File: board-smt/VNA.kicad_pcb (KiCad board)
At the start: 2 copper layers, 100 x 85 mm, 185 parts, among them J1 Conn_02x07_Odd_Even, J10 Conn_01x04, J11 Conn_01x01, J13 Barrel_Jack, J14 Conn_01x01, J15 Conn_01x02, J16 Conn_01x01, J18 Conn_01x01, J19 Conn_01x01, J2 Conn_Coaxial, J20 Conn_01x01, J21 Conn_01x01, J24 USB_B, J3 Conn_01x04, J8 Conn_01x01, J9 Conn_Coaxial, Q3 2SC3356, SW1 SW_DPDT_x2, SW2 SW_DIP_x01, U1 SI5351A, U10 MT3608, U11 CN3052, U12 SI5351A, U13 MicroSD_SPI_CD, U14 STM32F103C8T6, U2 LM393, U3 SA612, U4 SA612, U5 SA612, U6 LM358, U7 LM358, U8 AMS1117-3V3, U9 78M05_TO252, Y1 25 MHz, Y2 8 MHz

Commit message: Submitted to JLCPCB 2020-07-12
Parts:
- removed G***: LOGO, VNA:VNAOMizer
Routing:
- net GND: track 1891.0 -> 1892.7 mm
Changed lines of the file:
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@@
     (links 377)
     (no_connects 0)
-    (area 49.924999 49.924999 150.075001 135.075001)
+    (area 48.252381 38.824999 153.542859 144.065001)
     (thickness 1.6)
     (drawings 46)
     (tracks 3988)
     (zones 0)
-    (modules 185)
+    (modules 184)
     (nets 117)
   )
@@
   )
   (setup
-    (last_trace_width 0.35)
+    (last_trace_width 0.25)
     (user_trace_width 0.35)
     (user_trace_width 0.5)
@@
     (tags "capacitor 0805")
     (attr smd)
-    (fp_text reference C9 (at 1.7 1.7 360) (layer F.SilkS)
+    (fp_text reference C9 (at 2.89 0.13 360) (layer F.SilkS)
       (effects (font (size 1 1) (thickness 0.15)))
     )
@@
     (tags "capacitor 0805")
     (attr smd)
-    (fp_text reference C43 (at 3.048 -0.254 180) (layer F.SilkS)
+    (fp_text reference C43 (at 0.04 1.744 270) (layer F.SilkS)
       (effects (font (size 1 1) (thickness 0.15)))
     )
@@
     )
   )
-  (module VNA:VNAOMizer (layer F.Cu)
-    (at 113 96.3)
-    (fp_text reference G*** (at 0 0) (layer F.SilkS) hide
-      (effects (font (thickness 0.3)))
-    )
-    (fp_text value LOGO (at 0.75 0) (layer F.SilkS) hide
-      (effects (font (thickness 0.3)))
-    )
-    (fp_poly (pts (xy 0.293123 -4.621389) (xy 0.317894 -4.398101) (xy 0.334924 -4.059111) (xy 0.344295 -3.629613)
-      (xy 0.34609 -3.134799) (xy 0.340391 -2.599861) (xy 0.327282 -2.049993) (xy 0.306845 -1.510387)
-      (xy 0.281376 -1.040503) (xy 0.132851 0.549482) (xy -0.105598 2.051599) (xy -0.329137 3.068511)
-      (xy -0.44618 3.524507) (xy -0.548457 3.872163) (xy -0.646898 4.141893) (xy -0.752432 4.364109)
-      (xy -0.859182 4.543478) (xy -0.990915 4.742234) (xy -1.086976 4.877522) (xy -1.128467 4.922866)
-      (xy -1.128889 4.921308) (xy -1.107542 4.840305) (xy -1.050995 4.66136) (xy -0.970491 4.419781)
-      (xy -0.951308 4.363564) (xy -0.898844 4.199208) (xy -0.851171 4.020657) (xy -0.806283 3.813472)
-      (xy -0.76217 3.563215) (xy -0.716825 3.255448) (xy -0.668239 2.875732) (xy -0.614404 2.40963)
-      (xy -0.553313 1.842704) (xy -0.482956 1.160514) (xy -0.422889 0.564444) (xy -0.332038 -0.538475)
-      (xy -0.293424 -1.515472) (xy -0.307325 -2.371822) (xy -0.374021 -3.1128) (xy -0.49379 -3.743681)
-      (xy -0.666911 -4.269739) (xy -0.680017 -4.300431) (xy -0.776027 -4.552624) (xy -0.816049 -4.729629)
-      (xy -0.80382 -4.798291) (xy -0.705213 -4.833254) (xy -0.507852 -4.863601) (xy -0.254079 -4.882859)
-      (xy -0.248985 -4.883076) (xy 0.2416 -4.903612) (xy 0.293123 -4.621389)) (layer F.SilkS) (width 0.01))
-    (fp_poly (pts (xy 0.668263 1.317823) (xy 0.82314 1.450533) (xy 1.041855 1.651986) (xy 1.308286 1.906042)
-      (xy 1.606316 2.196557) (xy 1.919825 2.507389) (xy 2.232692 2.822398) (xy 2.5288 3.12544)
-      (xy 2.792028 3.400373) (xy 3.006256 3.631056) (xy 3.155366 3.801346) (xy 3.223238 3.895102)
-      (xy 3.225398 3.905751) (xy 3.182105 3.970047) (xy 3.099226 3.976528) (xy 2.956451 3.918004)
-      (xy 2.733471 3.787287) (xy 2.540815 3.663418) (xy 2.271595 3.49674) (xy 1.919779 3.292474)
-      (xy 1.529298 3.075503) (xy 1.144085 2.87071) (xy 1.112065 2.854184) (xy 0.211667 2.390755)
-      (xy 0.211667 2.035297) (xy 0.243772 1.767589) (xy 0.32785 1.526408) (xy 0.445544 1.34856)
-      (xy 0.578497 1.270853) (xy 0.593341 1.27) (xy 0.668263 1.317823)) (layer F.SilkS) (width 0.01))
-    (fp_poly (pts (xy -0.946216 1.065488) (xy -0.900925 1.10942) (xy -0.896299 1.223823) (xy -0.922406 1.442396)
-      (xy -0.924452 1.457488) (xy -0.981931 1.726207) (xy -1.064968 1.924752) (xy -1.10667 1.978735)
-      (xy -1.230238 2.049751) (xy -1.462247 2.143052) (xy -1.773553 2.249581) (xy -2.135011 2.360284)
-      (xy -2.517475 2.466105) (xy -2.891801 2.557989) (xy -3.139722 2.610395) (xy -3.407776 2.668996)
-      (xy -3.736706 2.750557) (xy -4.078508 2.84215) (xy -4.385181 2.930848) (xy -4.608723 3.003724)
-      (xy -4.630389 3.011827) (xy -4.715506 3.006539) (xy -4.727222 2.976652) (xy -4.750819 2.849293)
-      (xy -4.767361 2.799718) (xy -4.751137 2.730729) (xy -4.640454 2.649848) (xy -4.418805 2.54681)
-      (xy -4.255833 2.481694) (xy -3.959586 2.360263) (xy -3.572416 2.19175) (xy -3.129516 1.99238)
-      (xy -2.666076 1.778374) (xy -2.217289 1.565958) (xy -1.818347 1.371353) (xy -1.541823 1.23054)
-      (xy -1.318736 1.13034) (xy -1.1183 1.068245) (xy -1.042105 1.058333) (xy -0.946216 1.065488)) (layer F.SilkS) (width 0.01))
-    (fp_poly (pts (xy -0.542509 -1.64788) (xy -0.521421 -1.549341) (xy -0.530529 -1.363452) (xy -0.56247 -1.138882)
-      (xy -0.609884 -0.924303) (xy -0.665407 -0.768384) (xy -0.679048 -0.745207) (xy -0.798112 -0.65308)
-      (xy -1.042072 -0.532947) (xy -1.398515 -0.389323) (xy -1.855024 -0.226725) (xy -2.399185 -0.04967)
-      (xy -3.018582 0.137325) (xy -3.421944 0.252633) (xy -3.804445 0.360157) (xy -4.142102 0.455712)
-      (xy -4.410267 0.532274) (xy -4.584297 0.582817) (xy -4.636768 0.598905) (xy -4.747126 0.577683)
-      (xy -4.770388 0.551681) (xy -4.777941 0.491533) (xy -4.724056 0.417029) (xy -4.596658 0.320843)
-      (xy -4.38367 0.195646) (xy -4.073018 0.034112) (xy -3.652626 -0.171087) (xy -3.316111 -0.330735)
-      (xy -2.868776 -0.543522) (xy -2.396326 -0.771903) (xy -1.941683 -0.994892) (xy -1.54777 -1.191506)
-      (xy -1.367319 -1.283497) (xy -1.066596 -1.433976) (xy -0.812523 -1.552478) (xy -0.630213 -1.62791)
-      (xy -0.544776 -1.649177) (xy -0.542509 -1.64788)) (layer F.SilkS) (width 0.01))
-    (fp_poly (pts (xy 0.731539 -1.46223) (xy 0.818222 -1.415777) (xy 1.020676 -1.333993) (xy 1.319994 -1.223676)
-      (xy 1.69727 -1.091624) (xy 2.1336 -0.944634) (xy 2.54 -0.811992) (xy 3.1671 -0.606363)
-      (xy 3.667291 -0.433407) (xy 4.050033 -0.289514) (xy 4.324785 -0.171074) (xy 4.501006 -0.074478)
-      (xy 4.533195 -0.051462) (xy 4.689368 0.081748) (xy 4.784372 0.186969) (xy 4.797778 0.217595)
-      (xy 4.741426 0.270517) (xy 4.610175 0.272792) (xy 4.460733 0.22468) (xy 4.445 0.215962)
-      (xy 4.245346 0.135201) (xy 3.909109 0.045705) (xy 3.440487 -0.051644) (xy 2.843679 -0.155962)
-      (xy 2.222161 -0.251889) (xy 1.762746 -0.320933) (xy 1.421289 -0.377361) (xy 1.175812 -0.426708)
-      (xy 1.004335 -0.474508) (xy 0.884877 -0.526294) (xy 0.795458 -0.587601) (xy 0.758473 -0.620418)
-      (xy 0.608861 -0.816858) (xy 0.564488 -1.055794) (xy 0.564445 -1.065764) (xy 0.58005 -1.332126)
-      (xy 0.624665 -1.477904) (xy 0.694992 -1.495271) (xy 0.731539 -1.46223)) (layer F.SilkS) (width 0.01))
-  )
   (gr_text "AMS1117-\n3V3" (at 144.8 97.2 90) (layer F.SilkS)
     (effects (font (size 1 1) (thickness 0.15)))
@@
     (effects (font (size 1 1) (thickness 0.15)))
   )
-  (gr_text "VNA-O-MIZER BY D MARKS KW4TI,\nLICENSED UNDER CC-BY-SA 4.0" (at 83.9 103.3) (layer F.SilkS)
+  (gr_text "VNA-O-MIZER\nBY D MARKS KW4TI,\nLICENSED UNDER\nCC-BY-SA 4.0" (at 108.1 62.9) (layer F.SilkS)
     (effects (font (size 1 1) (thickness 0.15)))
   )
@@
   (via (at 60.4 70.8) (size 0.6) (drill 0.4) (layers F.Cu B.Cu) (net 2))
   (segment (start 60.45 70.95) (end 60.4 70.8) (width 0.35) (layer F.Cu) (net 2))
-  (segment (start 74.7 76.35) (end 74.65 77.55) (width 0.35) (layer F.Cu) (net 2))
-  (via (at 74.6 77.6) (size 0.6) (drill 0.4) (layers F.Cu B.Cu) (net 2))
-  (segment (start 74.65 77.55) (end 74.6 77.6) (width 0.35) (layer F.Cu) (net 2))
+  (segment (start 74.7 76.35) (end 73.57 76.45) (width 0.35) (layer F.Cu) (net 2))
+  (via (at 73.52 76.5) (size 0.6) (drill 0.4) (layers F.Cu B.Cu) (net 2))
+  (segment (start 73.57 76.45) (end 73.52 76.5) (width 0.35) (layer F.Cu) (net 2))
   (segment (start 74.7 76.35) (end 75.35 76.35) (width 0.35) (layer F.Cu) (net 2))
   (via (at 75.8 76.8) (size 0.6) (drill 0.4) (layers F.Cu B.Cu) (net 2))
@@
   (via (at 96.6 119.5) (size 0.6) (drill 0.4) (layers F.Cu B.Cu) (net 2))
   (segment (start 85.45 121.45) (end 84.62 121.45) (width 0.35) (layer F.Cu) (net 2))
-  (segment (start 84.348 107.97) (end 84.836 108.458) (width 0.5) (layer F.Cu) (net 2))
-  (via (at 84.836 108.458) (size 0.6) (drill 0.4) (layers F.Cu B.Cu) (net 2))
+  (segment (start 84.348 107.97) (end 84.84 107.38) (width 0.5) (layer F.Cu) (net 2))
+  (via (at 84.84 107.38) (size 0.6) (drill 0.4) (layers F.Cu B.Cu) (net 2))
   (segment (start 83.566 107.97) (end 84.348 107.97) (width 0.5) (layer F.Cu) (net 2))
   (via (at 85.45 121.45) (size 0.6) (drill 0.4) (layers F.Cu B.Cu) (net 2))
@@
   (segment (start 85.3 111.15) (end 85.2 111.25) (width 0.35) (layer B.Cu) (net 2))
   (via (at 85.3 111.15) (size 0.6) (drill 0.4) (layers F.Cu B.Cu) (net 2))
-  (segment (start 85.2 109.4) (end 85.3 111.15) (width 0.35) (layer F.Cu) (net 2))
-  (segment (start 85.3 109.3) (end 85.2 109.4) (width 0.35) (layer F.Cu) (net 2))
-  (via (at 85.3 109.3) (size 0.6) (drill 0.4) (layers F.Cu B.Cu) (net 2))
-  (segment (start 84.958 108.458) (end 85.3 109.3) (width 0.35) (layer B.Cu) (net 2))
-  (segment (start 84.836 108.458) (end 84.958 108.458) (width 0.35) (layer B.Cu) (net 2))
+  (segment (start 86.23 109.31) (end 85.3 111.15) (width 0.35) (layer F.Cu) (net 2))
+  (segment (start 86.33 109.21) (end 86.23 109.31) (width 0.35) (layer F.Cu) (net 2))
+  (via (at 86.33 109.21) (size 0.6) (drill 0.4) (layers F.Cu B.Cu) (net 2))
+  (segment (start 84.962 107.38) (end 86.33 109.21) (width 0.35) (layer B.Cu) (net 2))
+  (segment (start 84.84 107.38) (end 84.962 107.38) (width 0.35) (layer B.Cu) (net 2))
   (segment (start 84.62 121.45) (end 84.582 121.412) (width 0.35) (layer F.Cu) (net 2))
   (segment (start 84.8 128.2) (end 84.8 127.6) (width 0.35) (layer B.Cu) (net 2))

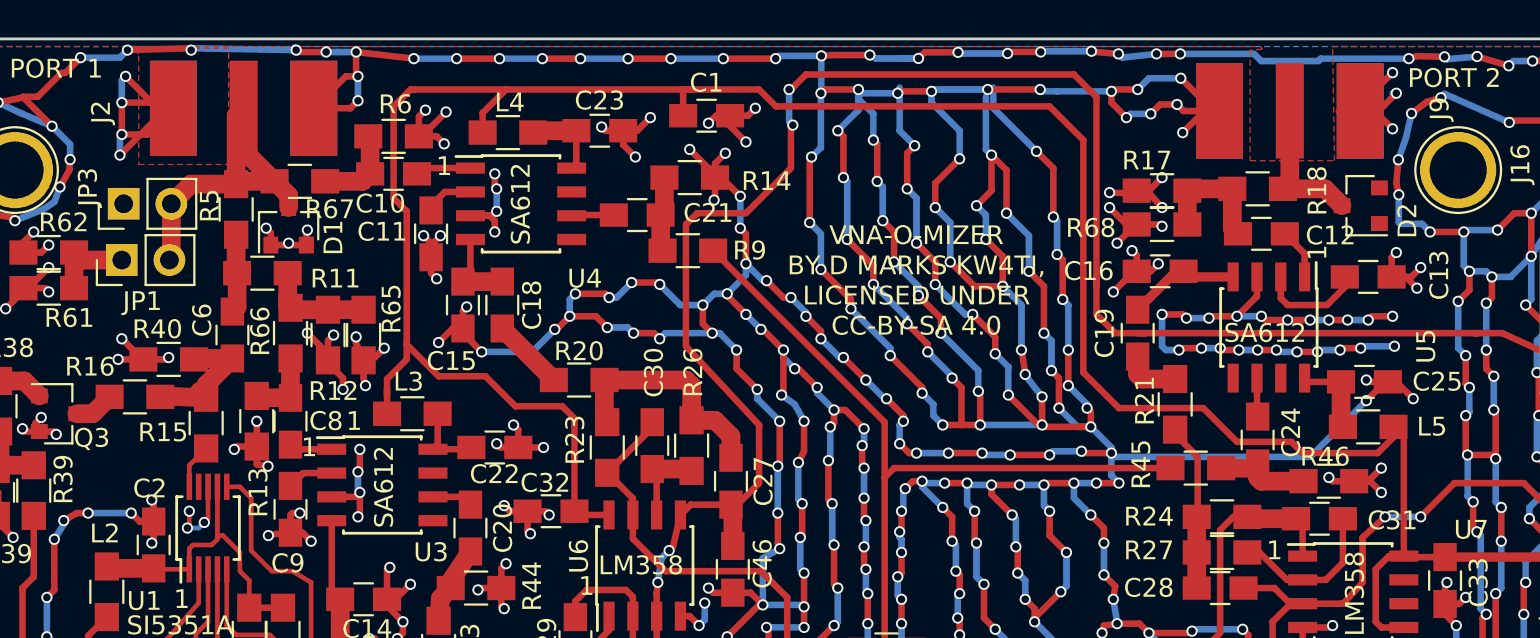
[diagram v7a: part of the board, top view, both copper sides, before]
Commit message: Modified some component values on bridge for better performance
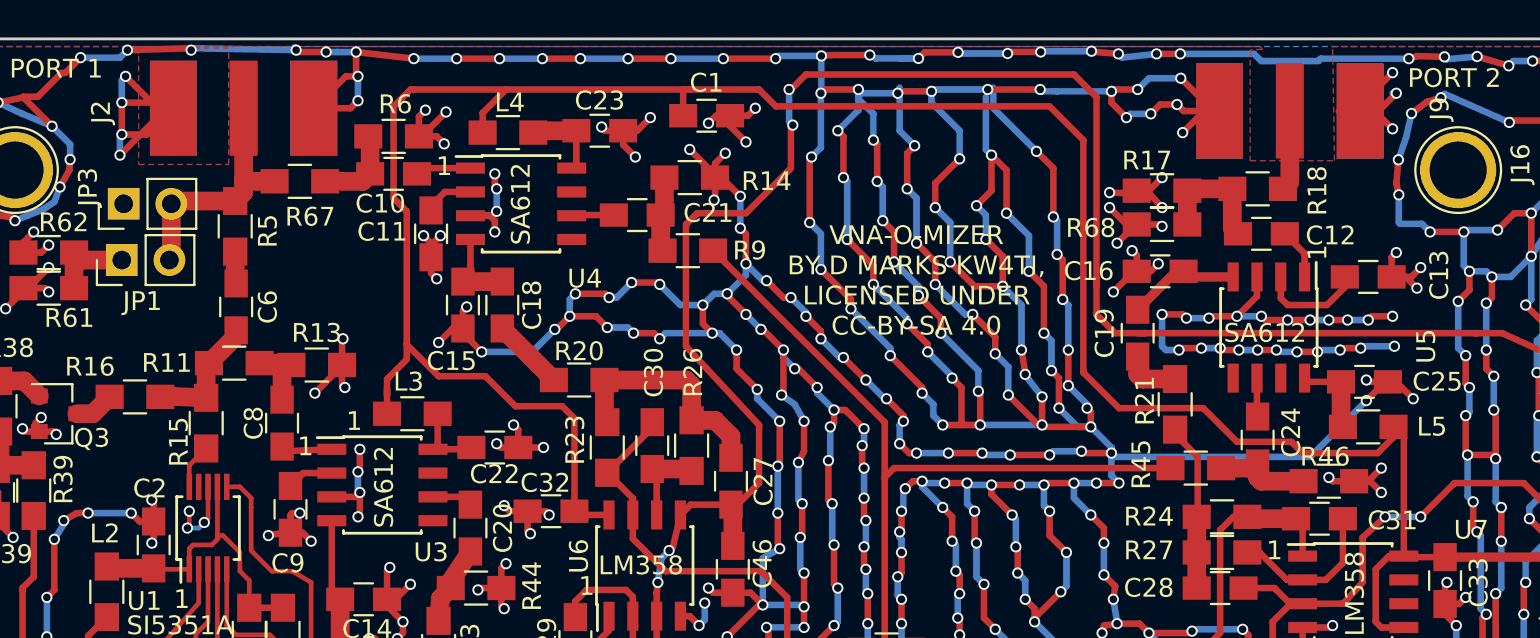
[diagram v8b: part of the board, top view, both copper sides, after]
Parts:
- removed D1, D2: BAV99, TO_SOT_Packages_SMD:SOT-23
- removed R12, R40, R65: 100R, Resistors_SMD:R_0805_HandSoldering
- removed R66: 120R, Resistors_SMD:R_0805_HandSoldering
- R11: value 47R -> 82R
- R13, R6: value 4R7 -> 1R
- R15: value 220R -> 51R
- R5: value 47R -> 51R
- R68: value 22R -> 1R
- moved R11 5.03 mm to (71.7, 67.3)
- moved R13 4.39 mm to (76.1, 67.4), turned to 0 degrees
- moved C6 1.51 mm to (71.8, 64.3)
- moved R5 0.90 mm to (71.8, 60.0)
- moved C8 0.46 mm to (74.2, 70.5)
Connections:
- C6 pad 1: Net-(C6-Pad1) -> CLK0
- C6 pad 2: CLK0 -> Net-(C6-Pad2)
- R11 pad 1: Net-(R11-Pad1) -> SAMPVOLT
- R15 pad 1: Net-(C6-Pad1) -> CLK0
- R16 pad 1: Net-(C6-Pad1) -> CLK0
- R5 pad 2: CLK0 -> Net-(C6-Pad2)
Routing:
- net GND: track 1892.7 -> 1875.6 mm, vias 797 -> 785
- net Net-(C6-Pad1): track 7.72 -> 0.00 mm
- net Net-(J2-Pad1): track 19.6 -> 13.7 mm
- net Net-(R11-Pad1): track 5.85 -> 0.00 mm
- net Net-(J9-Pad1): track 9.91 -> 6.39 mm
- net CLK0: track 4.22 -> 6.74 mm
- net Net-(C6-Pad2): track 0.00 -> 1.72 mm
